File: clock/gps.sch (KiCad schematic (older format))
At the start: 9 parts, among them P301 MCRF, U301 Adafruit746, U302 MIC5225, U303 PA6H

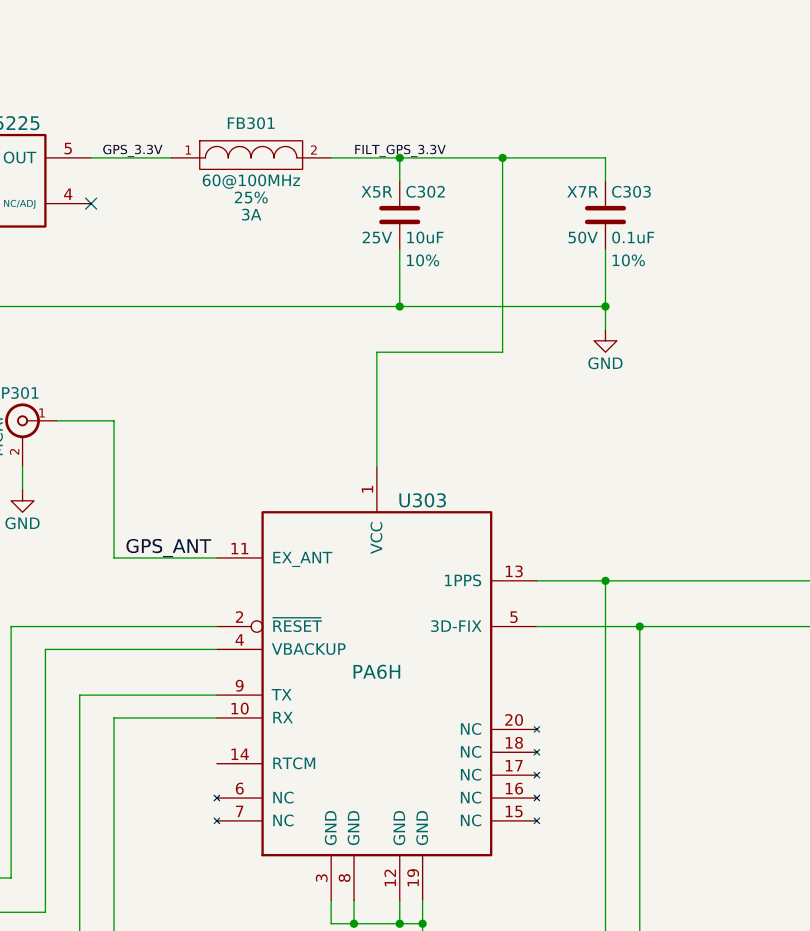
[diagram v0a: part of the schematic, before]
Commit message: Clean up most of the schematic DRC errors. Update placement.
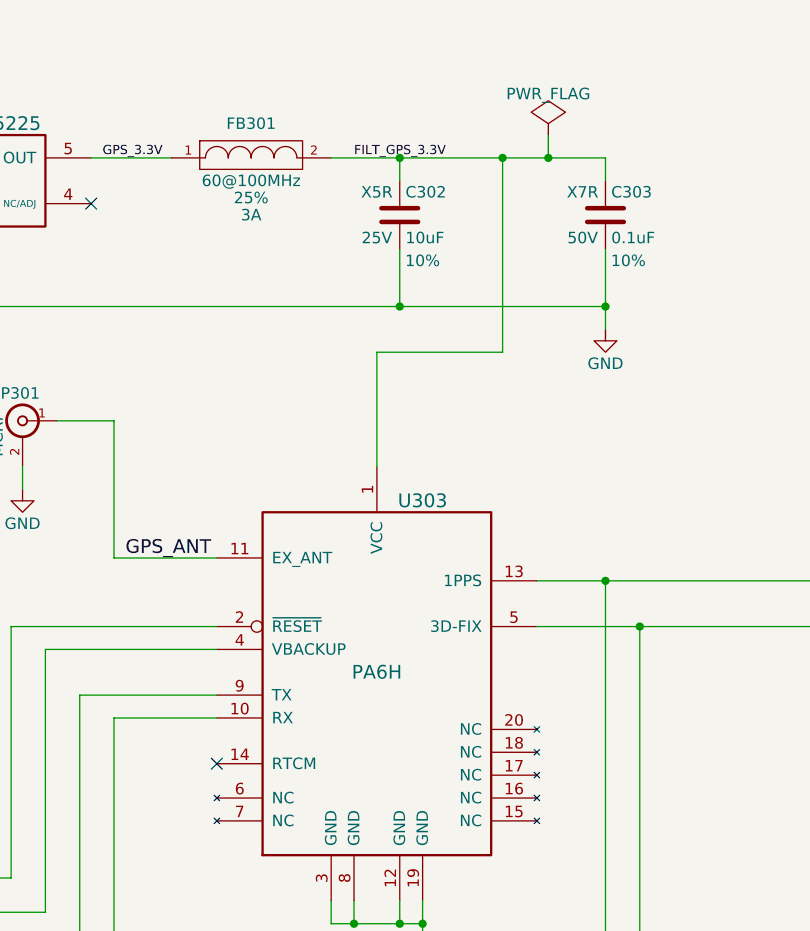
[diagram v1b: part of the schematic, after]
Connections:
- no-connect marks 2 -> 3
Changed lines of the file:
@@
 Text Label 6900 1900 0    40   ~ 0
 FILT_GPS_3.3V
+$Comp
+L PWR_FLAG #FLG049
+U 1 1 5643829E
+P 7750 1800
+F 0 "#FLG049" H 7750 1895 50  0001 C CNN
+F 1 "PWR_FLAG" H 7750 1980 50  0000 C CNN
+F 2 "" H 7750 1800 60  0000 C CNN
+F 3 "" H 7750 1800 60  0000 C CNN
+	1    7750 1800
+	1    0    0    -1
+$EndComp
+Wire Wire Line
+	7750 1800 7750 1900
+Connection ~ 7750 1900
+NoConn ~ 6300 4550
 $EndSCHEMATC

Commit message: Checkpoint... Pin swaps on microzed connector.
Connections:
- net ~RESET~: now reaches U301.8 (ENABLE), U303.2 (~RESET~)
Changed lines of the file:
@@
 Connection ~ 7750 1900
 NoConn ~ 6300 4550
+Text Label 4250 5050 0    60   ~ 0
+~RESET~
 $EndSCHEMATC

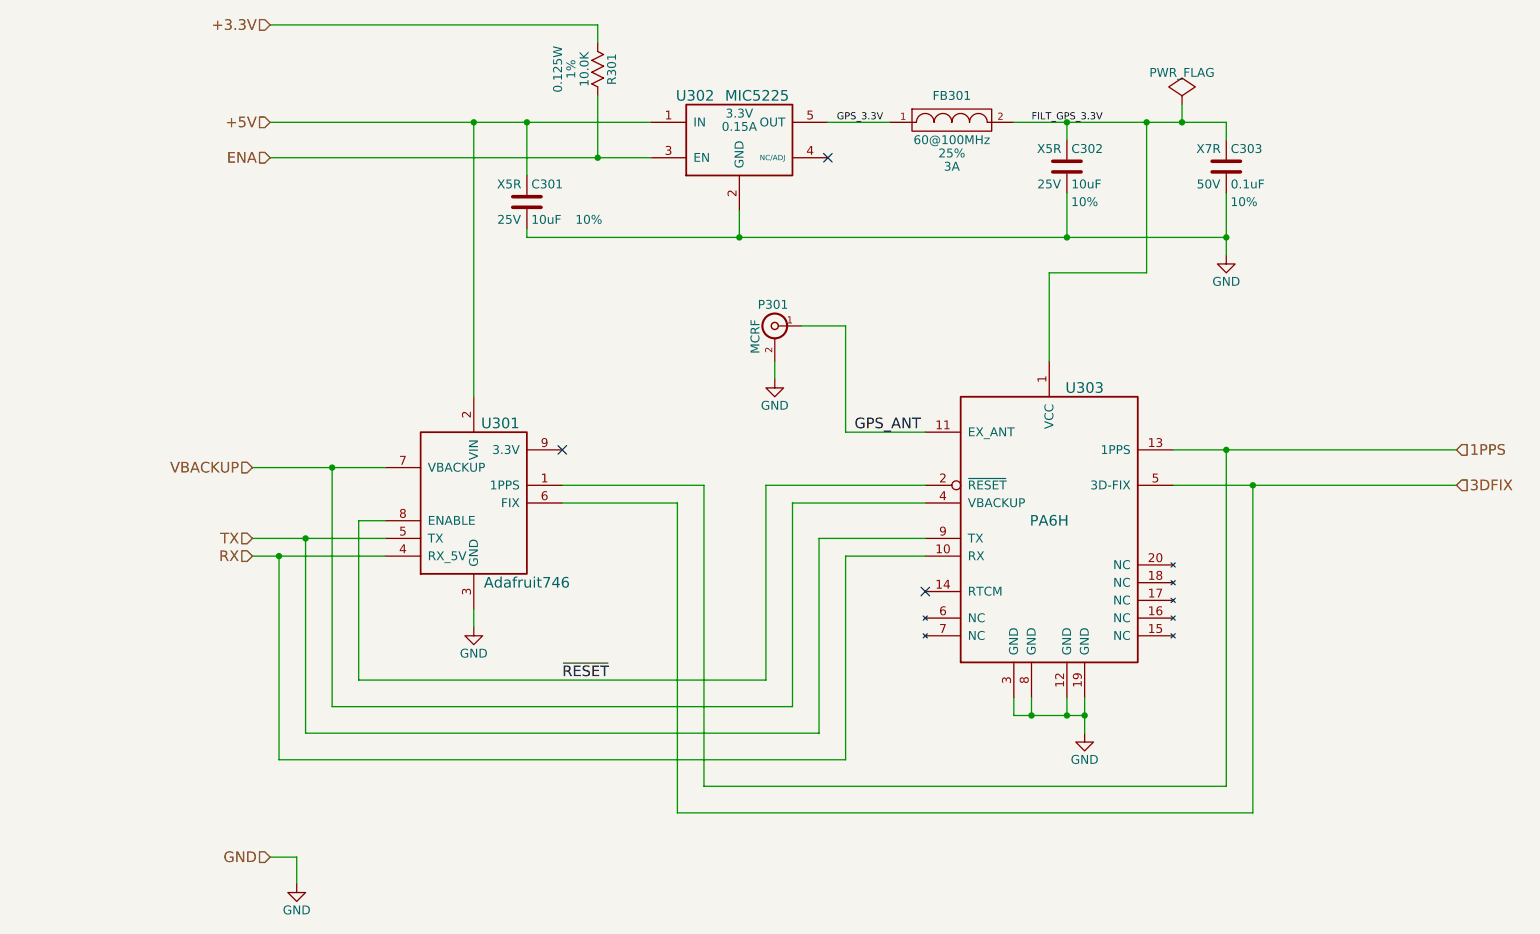
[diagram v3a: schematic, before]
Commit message: Preliminary changes from lab bring up.   Properly connect ref2 on PCA9306.   Duplicate +5V power good to drive +3.3V converter.   Change gain structure on OCXO control voltage drive.   Add FET control to disable linear regulators.
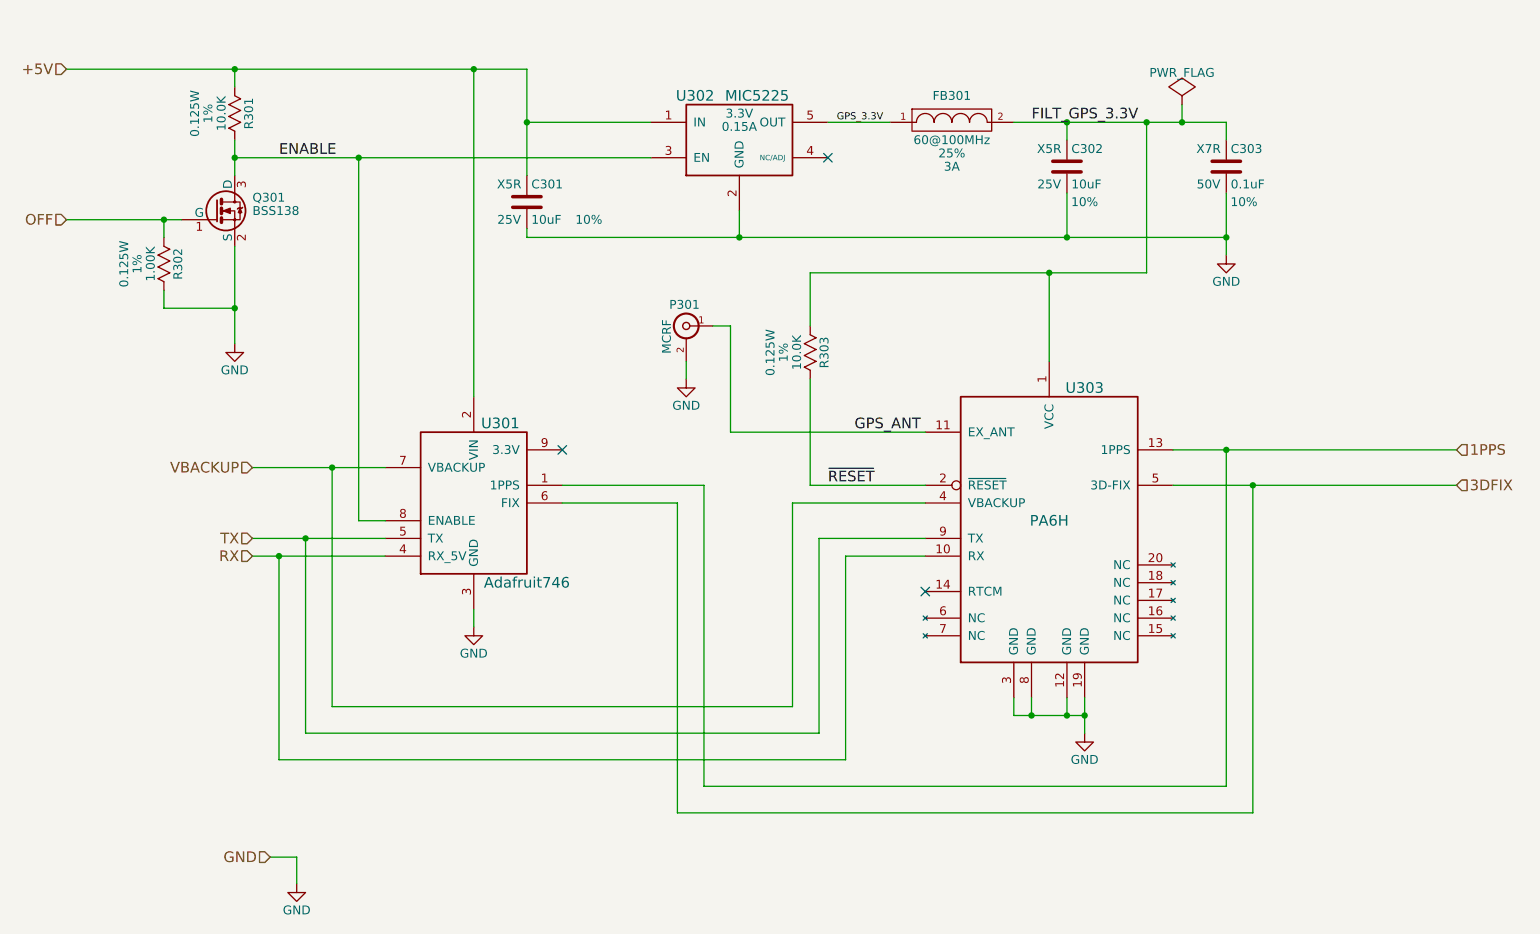
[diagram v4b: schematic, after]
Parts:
- added Q301: BSS138, local:SOT-23-3_NXP_HandSoldering, symbol BSS138
- added R302: 1.00K, Resistors_SMD:R_0805_HandSoldering, symbol R_local
- added R303: 10.0K, Resistors_SMD:R_0805_HandSoldering, symbol R_local
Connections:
- net +3.3V is gone; now on net +5V: R301.1
- net FILT_GPS_3.3V: now also R303.1
- net GND: now also Q301.2 (S), R302.2
- net ~RESET~: now also R303.2; no longer U301.8 (ENABLE)
- net ENA renamed ENABLE
- net ENABLE: now also U301.8 (ENABLE), Q301.3 (D)
- new net OFF: Q301.1 (G), R302.1
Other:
- moved on the sheet: P301, R301
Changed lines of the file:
@@
 L BNC P301
 U 1 1 561A3335
-P 5450 3050
-F 0 "P301" H 5460 3170 50  0000 C CNN
-F 1 "MCRF" V 5560 2990 50  0000 C CNN
-F 2 "local:MCRF_73412" H 5450 3050 60  0001 C CNN
-F 3 "" H 5450 3050 60  0000 C CNN
-F 4 "Molex" H 5450 3050 50  0001 C CNN "Manufacturer"
-F 5 "073412-0110" H 5450 3050 50  0001 C CNN "PartNum"
-	1    5450 3050
+P 4950 3050
+F 0 "P301" H 4960 3170 50  0000 C CNN
+F 1 "MCRF" V 5060 2990 50  0000 C CNN
+F 2 "local:MCRF_73412" H 4950 3050 60  0001 C CNN
+F 3 "" H 4950 3050 60  0000 C CNN
+F 4 "Molex" H 4950 3050 50  0001 C CNN "Manufacturer"
+F 5 "073412-0110" H 4950 3050 50  0001 C CNN "PartNum"
+	1    4950 3050
 	-1   0    0    -1
 $EndComp
 $Comp
-L GND #PWR040
+L GND #PWR305
 U 1 1 56235A8F
 P 7200 5350
-F 0 "#PWR040" H 7200 5100 50  0001 C CNN
+F 0 "#PWR305" H 7200 5100 50  0001 C CNN
 F 1 "GND" H 7200 5200 50  0000 C CNN
 F 2 "" H 7200 5350 60  0000 C CNN
@@
 Connection ~ 7100 1900
 $Comp
-L GND #PWR041
+L GND #PWR306
 U 1 1 56235D57
 P 8000 2650
-F 0 "#PWR041" H 8000 2400 50  0001 C CNN
+F 0 "#PWR306" H 8000 2400 50  0001 C CNN
 F 1 "GND" H 8000 2500 50  0000 C CNN
 F 2 "" H 8000 2650 60  0000 C CNN
@@
 $EndComp
 Wire Wire Line
-	2600 1900 4750 1900
-Wire Wire Line
-	4050 1900 4050 2200
-Connection ~ 4050 1900
+	1450 1600 4050 1600
+Wire Wire Line
+	4050 1900 4750 1900
+Wire Wire Line
+	4050 1600 4050 2200
 Wire Wire Line
 	4050 2500 4050 2550
@@
 Connection ~ 7100 2550
 Wire Wire Line
-	4450 1750 4450 2100
-Wire Wire Line
-	2600 2100 4750 2100
-Wire Wire Line
-	4450 1450 4450 1350
-Wire Wire Line
-	4450 1350 2600 1350
-Connection ~ 4450 2100
-Text HLabel 2600 1900 0    60   Input ~ 0
+	2400 2000 2400 2200
+Wire Wire Line
+	2400 2100 4750 2100
+Connection ~ 2400 2100
+Text HLabel 1450 1600 0    60   Input ~ 0
 +5V
-Text HLabel 2600 2100 0    60   Input ~ 0
-ENA
-Text HLabel 2600 1350 0    60   Input ~ 0
-+3.3V
+Text HLabel 1450 2450 0    60   Input ~ 0
+OFF
 Text HLabel 2500 4250 0    60   Input ~ 0
 TX
@@
 RX
 Wire Wire Line
-	5600 3050 5850 3050
-Wire Wire Line
-	5850 3050 5850 3650
-Wire Wire Line
-	5850 3650 6300 3650
-$Comp
-L GND #PWR042
+	5100 3050 5200 3050
+Wire Wire Line
+	5200 3050 5200 3650
+Wire Wire Line
+	5200 3650 6300 3650
+$Comp
+L GND #PWR304
 U 1 1 56236310
-P 5450 3350
-F 0 "#PWR042" H 5450 3100 50  0001 C CNN
-F 1 "GND" H 5450 3200 50  0000 C CNN
-F 2 "" H 5450 3350 60  0000 C CNN
-F 3 "" H 5450 3350 60  0000 C CNN
-	1    5450 3350
-	1    0    0    -1
-$EndComp
-Wire Wire Line
-	5450 3350 5450 3250
+P 4950 3350
+F 0 "#PWR304" H 4950 3100 50  0001 C CNN
+F 1 "GND" H 4950 3200 50  0000 C CNN
+F 2 "" H 4950 3350 60  0000 C CNN
+F 3 "" H 4950 3350 60  0000 C CNN
+	1    4950 3350
+	1    0    0    -1
+$EndComp
+Wire Wire Line
+	4950 3350 4950 3250
 Wire Wire Line
 	2500 4250 3250 4250
@@
 	2500 3850 3250 3850
 $Comp
-L GND #PWR043
+L GND #PWR303
 U 1 1 56236487
 P 3750 4750
-F 0 "#PWR043" H 3750 4500 50  0001 C CNN
+F 0 "#PWR303" H 3750 4500 50  0001 C CNN
 F 1 "GND" H 3750 4600 50  0000 C CNN
 F 2 "" H 3750 4750 60  0000 C CNN
@@
 Connection ~ 8150 3950
 Wire Wire Line
-	3750 3450 3750 1900
-Connection ~ 3750 1900
+	3750 3450 3750 1600
+Connection ~ 3750 1600
 Wire Wire Line
 	7000 3250 7000 2750
 Wire Wire Line
-	7000 2750 7550 2750
+	5650 2750 7550 2750
 Wire Wire Line
 	7550 2750 7550 1900
@@
 GND
 $Comp
-L GND #PWR044
+L GND #PWR302
 U 1 1 5624967B
 P 2750 6200
-F 0 "#PWR044" H 2750 5950 50  0001 C CNN
+F 0 "#PWR302" H 2750 5950 50  0001 C CNN
 F 1 "GND" H 2750 6050 50  0000 C CNN
 F 2 "" H 2750 6200 60  0000 C CNN
@@
 $EndComp
 Wire Wire Line
-	6300 3950 5400 3950
-Wire Wire Line
-	5400 3950 5400 5050
-Wire Wire Line
-	5400 5050 3100 5050
-Wire Wire Line
-	3100 5050 3100 4150
-Wire Wire Line
-	3100 4150 3250 4150
+	6300 3950 5650 3950
 $Comp
 L R_local R301
 U 1 1 5632AC0C
-P 4450 1600
-F 0 "R301" V 4530 1600 50  0000 C CNN
-F 1 "10.0K" V 4375 1600 50  0000 C CNN
-F 2 "Resistors_SMD:R_0805_HandSoldering" V 4380 1600 30  0001 C CNN
-F 3 "" V 4530 1600 30  0000 C CNN
-F 4 "1%" V 4300 1600 50  0000 C CNN "Tolerance"
-F 5 "0.125W" V 4225 1600 50  0000 C CNN "Power"
-F 6 "Vishay Dale" V 4450 1600 50  0001 C CNN "Manufacturer"
-F 7 "CRCW080510K0FKEA" V 4600 1600 50  0001 C CNN "PartNum"
-	1    4450 1600
+P 2400 1850
+F 0 "R301" V 2480 1850 50  0000 C CNN
+F 1 "10.0K" V 2325 1850 50  0000 C CNN
+F 2 "Resistors_SMD:R_0805_HandSoldering" V 2330 1850 30  0001 C CNN
+F 3 "" V 2480 1850 30  0000 C CNN
+F 4 "1%" V 2250 1850 50  0000 C CNN "Tolerance"
+F 5 "0.125W" V 2175 1850 50  0000 C CNN "Power"
+F 6 "Vishay Dale" V 2400 1850 50  0001 C CNN "Manufacturer"
+F 7 "CRCW080510K0FKEA" V 2550 1850 50  0001 C CNN "PartNum"
+	1    2400 1850
 	1    0    0    -1
 $EndComp
@@
 Text Label 5800 1900 0    40   ~ 0
 GPS_3.3V
-Text Label 6900 1900 0    40   ~ 0
+Text Label 6900 1900 0    60   ~ 0
 FILT_GPS_3.3V
 $Comp
-L PWR_FLAG #FLG045
+L PWR_FLAG #FLG301
 U 1 1 5643829E
 P 7750 1800
-F 0 "#FLG045" H 7750 1895 50  0001 C CNN
+F 0 "#FLG301" H 7750 1895 50  0001 C CNN
 F 1 "PWR_FLAG" H 7750 1980 50  0000 C CNN
 F 2 "" H 7750 1800 60  0000 C CNN
@@
 Connection ~ 7750 1900
 NoConn ~ 6300 4550
-Text Label 4250 5050 0    60   ~ 0
+Text Label 5750 3950 0    60   ~ 0
 ~RESET~
+$Comp
+L BSS138 Q301
+U 1 1 57AB6857
+P 2300 2400
+F 0 "Q301" H 2500 2475 50  0000 L CNN
+F 1 "BSS138" H 2500 2400 50  0000 L CNN
+F 2 "local:SOT-23-3_NXP_HandSoldering" H 2500 2325 50  0001 L CIN
+F 3 "" H 2300 2400 50  0000 L CNN
+F 4 "ON Semiconductor" H 2300 2400 60  0001 C CNN "Manufacturer"
+F 5 "BSS138LT1G" H 2300 2400 60  0001 C CNN "PartNum"
+	1    2300 2400
+	1    0    0    -1
+$EndComp
+Wire Wire Line
+	2400 1700 2400 1600
+Connection ~ 2400 1600
+Connection ~ 4050 1900
+Wire Wire Line
+	1450 2450 2100 2450
+$Comp
+L GND #PWR301
+U 1 1 57AB6F8A
+P 2400 3150
+F 0 "#PWR301" H 2400 2900 50  0001 C CNN
+F 1 "GND" H 2400 3000 50  0000 C CNN
+F 2 "" H 2400 3150 60  0000 C CNN
+F 3 "" H 2400 3150 60  0000 C CNN
+	1    2400 3150
+	1    0    0    -1
+$EndComp
+Wire Wire Line
+	2400 2600 2400 3150
+$Comp
+L R_local R302
+U 1 1 57AB6FA9
+P 2000 2700
+F 0 "R302" V 2080 2700 50  0000 C CNN
+F 1 "1.00K" V 1925 2700 50  0000 C CNN
+F 2 "Resistors_SMD:R_0805_HandSoldering" V 1930 2700 30  0001 C CNN
+F 3 "" V 2080 2700 30  0000 C CNN
+F 4 "1%" V 1850 2700 50  0000 C CNN "Tolerance"
+F 5 "0.125W" V 1775 2700 50  0000 C CNN "Power"
+F 6 "Vishay Dale" V 2000 2700 50  0001 C CNN "Manufacturer"
+F 7 "CRCW080510K0FKEA" V 2150 2700 50  0001 C CNN "PartNum"
+	1    2000 2700
+	1    0    0    -1
+$EndComp
+Wire Wire Line
+	2000 2550 2000 2450
+Connection ~ 2000 2450
+Wire Wire Line
+	2000 2850 2000 2950
+Wire Wire Line
+	2000 2950 2400 2950
+Connection ~ 2400 2950
+Connection ~ 3100 2100
+Wire Wire Line
+	3250 4150 3100 4150
+Wire Wire Line
+	3100 4150 3100 2100
+$Comp
+L R_local R303
+U 1 1 57AB756F
+P 5650 3200
+F 0 "R303" V 5730 3200 50  0000 C CNN
+F 1 "10.0K" V 5575 3200 50  0000 C CNN
+F 2 "Resistors_SMD:R_0805_HandSoldering" V 5580 3200 30  0001 C CNN
+F 3 "" V 5730 3200 30  0000 C CNN
+F 4 "1%" V 5500 3200 50  0000 C CNN "Tolerance"
+F 5 "0.125W" V 5425 3200 50  0000 C CNN "Power"
+F 6 "Vishay Dale" V 5650 3200 50  0001 C CNN "Manufacturer"
+F 7 "CRCW080510K0FKEA" V 5800 3200 50  0001 C CNN "PartNum"
+	1    5650 3200
+	1    0    0    -1
+$EndComp
+Wire Wire Line
+	5650 3950 5650 3350
+Wire Wire Line
+	5650 3050 5650 2750
+Connection ~ 7000 2750
+Text Label 2650 2100 0    60   ~ 0
+ENABLE
 $EndSCHEMATC
